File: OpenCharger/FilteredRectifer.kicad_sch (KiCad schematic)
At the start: 6 parts, among them Q1 IPT015N10N5, Q2 IPT015N10N5, Q3 IPT015N10N5, Q4 IPT015N10N5

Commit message: updated
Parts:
- added C12, C13, C5, C9: 100uF, Capacitor_THT:CP_Radial_D16.0mm_P7.50mm, symbol Device:C_Polarized_US
- added D2, D3: D_Zener, symbol Device:D_Zener
- added Q10, Q11, Q12, Q13, Q14, Q15, Q16, Q17: IPT015N10N5, Package_TO_SOT_SMD:Infineon_PG-HSOF-8-1, symbol Transistor_FET:IPT015N10N5
- added R14, R15, R2, R4: R_US, Resistor_SMD:R_0603_1608Metric, symbol Device:R_US
- added R3: R_Small_US, symbol Device:R_Small_US
- added U4: MCP6L01x-xLT, Package_TO_SOT_SMD:SOT-353_SC-70-5, symbol Amplifier_Operational:MCP6L01x-xLT
- C3, C4: value 56uF -> 100uF; footprint Capacitor_THT:CP_Radial_D40.0mm_P10.00mm_SnapIn -> Capacitor_THT:CP_Radial_D16.0mm_P7.50mm
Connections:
- net V_{in}+: now also Q10.3 (D), R2.1; no longer Q1.3 (D)
- net V_{in}-: now also Q15.2 (S), R4.2; no longer Q2.2 (S)
- net V_{out}+: now also Q1.3 (D), C12.1, C13.1, C5.1, C9.1, Q13.3 (D); no longer Q2.3 (D), Q3.3 (D)
- net V_{out}-: now also C12.2, C13.2, C5.2, C9.2, D2.2 (A), D3.2 (A), Q12.2 (S), Q17.2 (S), R14.2, R15.1, U4.2 (V-); no longer Q1.2 (S), Q4.2 (S)
- net PHG2: now reaches Q1.1 (G)
- net PHG0: now reaches Q3.1 (G)
- net NLG2: now reaches Q4.1 (G)
- net PHG1: now reaches Q2.1 (G)
- new net: D3.1 (K), R15.2, R3.2, R4.1, U4.4 (-)
- new net: D2.1 (K), R14.1, R2.2, R3.1, U4.3 (+)
- new net 3v3: U4.5 (V+)
- new net FORWARD: U4.1
- new net NHG0: Q15.1 (G)
- new net NHG1: Q14.1 (G)
- new net NHG2: Q13.1 (G)
- new net NHS1: Q14.2 (S), Q15.3 (D)
- new net NHS2: Q13.2 (S), Q14.3 (D)
- new net NLG0: Q17.1 (G)
- new net NLG1: Q16.1 (G)
- new net NLS1: Q16.2 (S), Q17.3 (D)
- new net NLS2: Q16.3 (D), Q4.2 (S)
- new net PHS1: Q2.2 (S), Q3.3 (D)
- new net PHS2: Q1.2 (S), Q2.3 (D)
- new net PLG0: Q12.1 (G)
- new net PLG1: Q11.1 (G)
- new net PLG2: Q10.1 (G)
- new net PLS1: Q11.2 (S), Q12.3 (D)
- new net PLS2: Q10.2 (S), Q11.3 (D)
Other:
- added sheet Rectifier Gate Drivers (RectifierGateDrivers.kicad_sch)
- note added: "Diode Enable"
- moved on the sheet: Q3, Q4

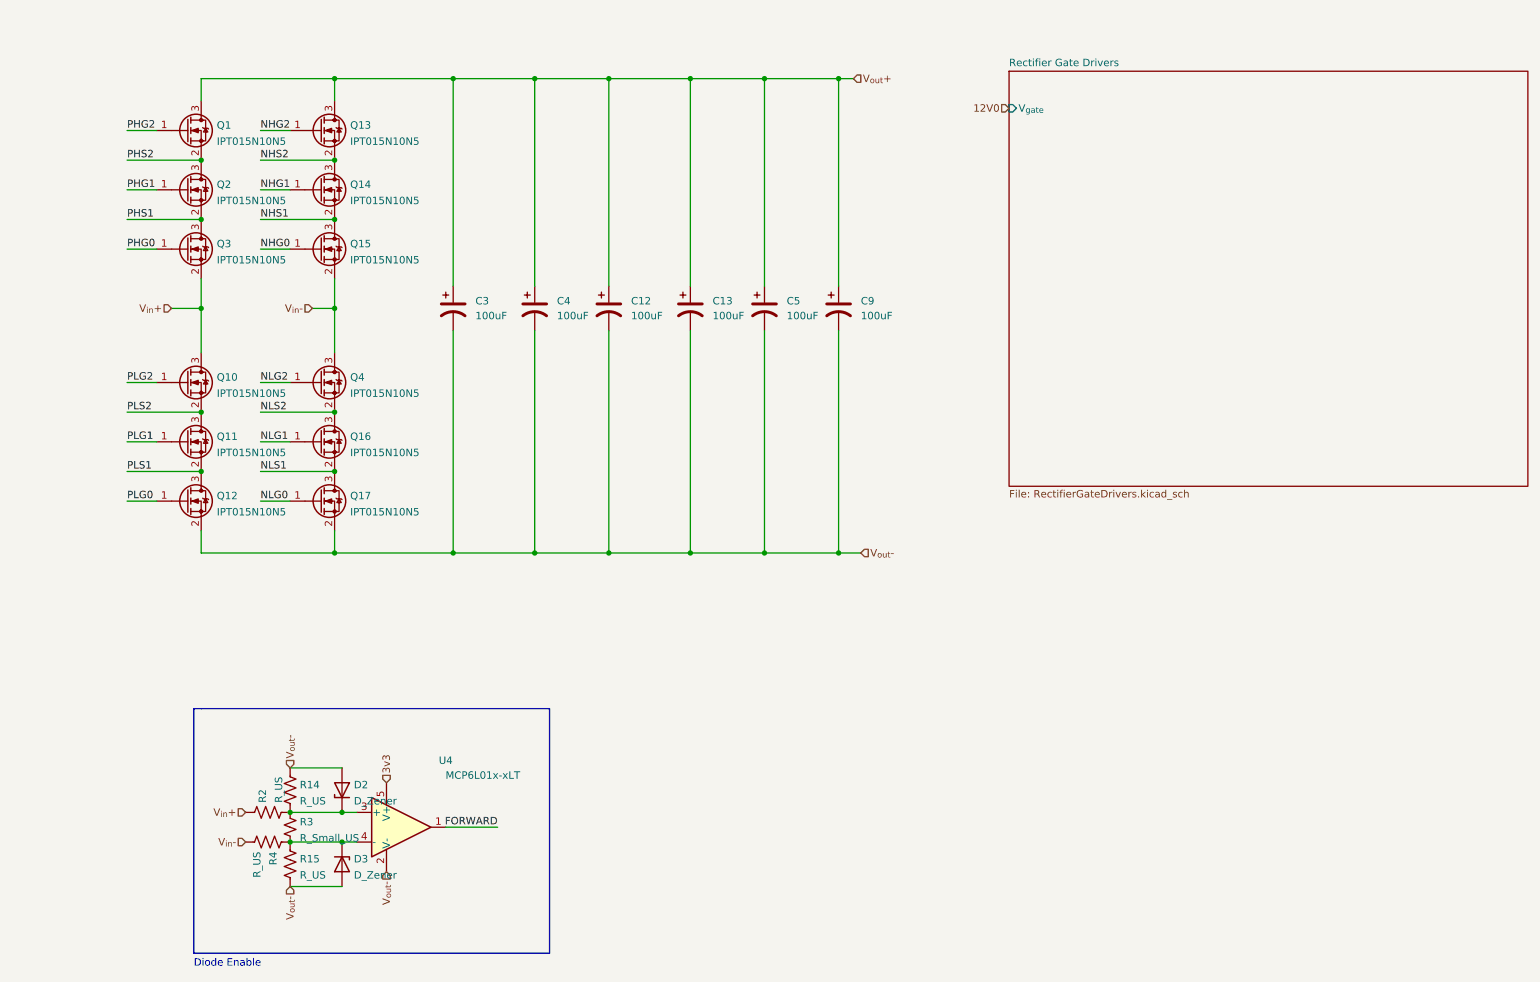
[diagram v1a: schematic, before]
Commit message: Updated Charger and MC
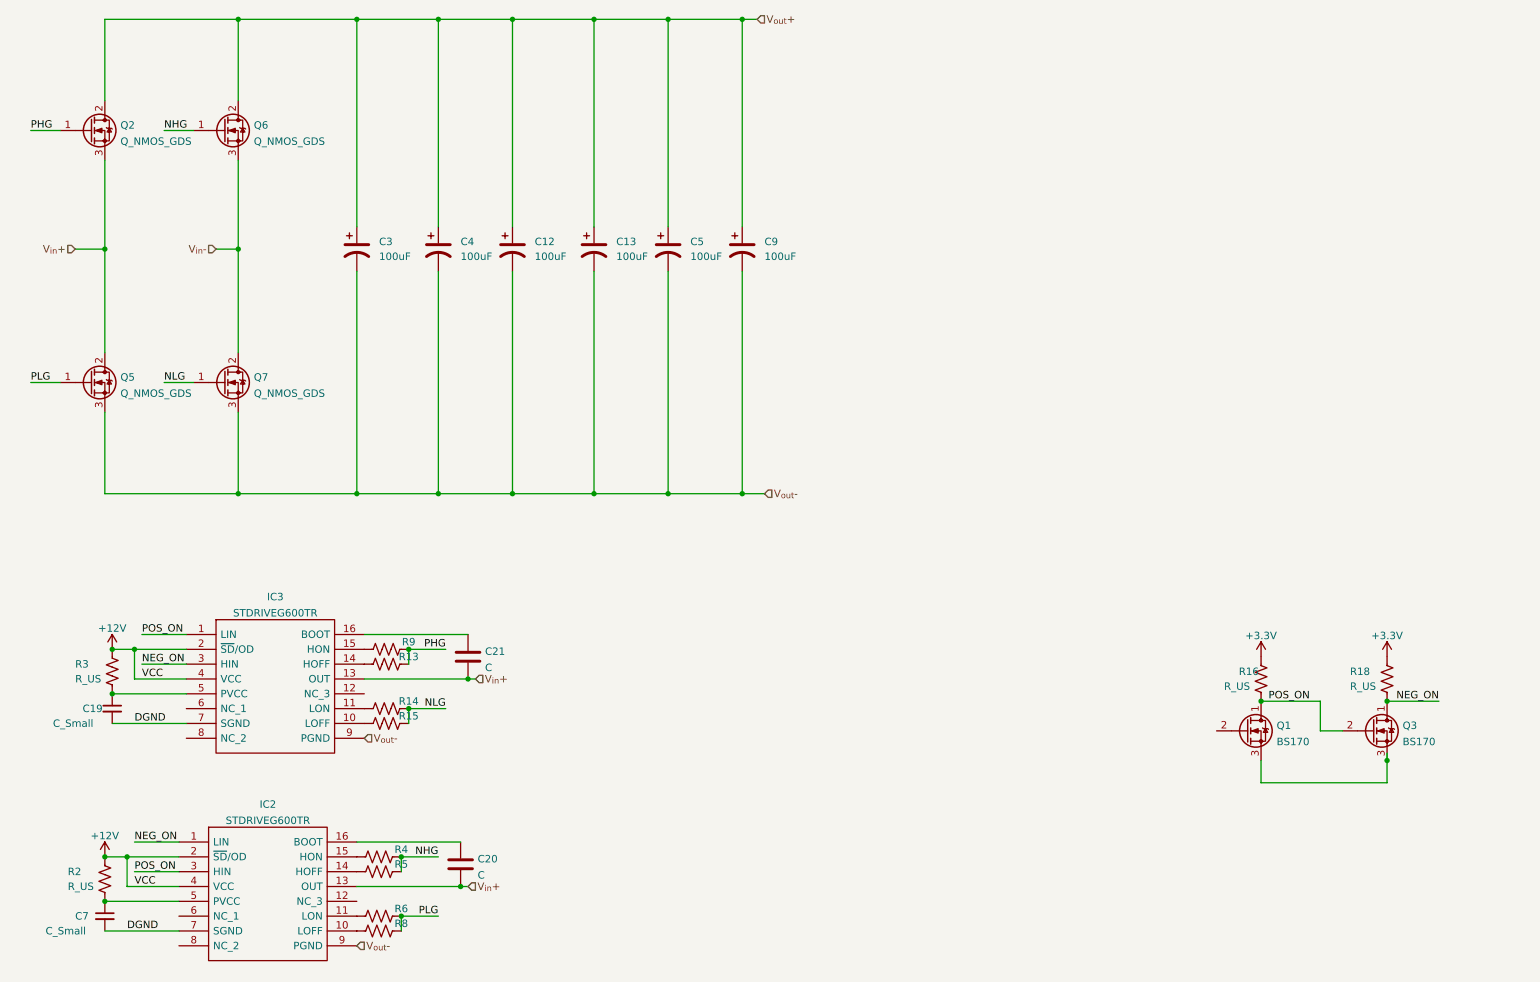
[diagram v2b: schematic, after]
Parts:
- removed D2, D3: D_Zener, symbol Device:D_Zener
- removed Q1, Q10, Q11, Q12, Q13, Q14, Q15, Q16, Q17, Q2, Q3, Q4: IPT015N10N5, Package_TO_SOT_SMD:Infineon_PG-HSOF-8-1, symbol Transistor_FET:IPT015N10N5
- removed R3: R_Small_US, symbol Device:R_Small_US
- removed U4: MCP6L01x-xLT, Package_TO_SOT_SMD:SOT-353_SC-70-5, symbol Amplifier_Operational:MCP6L01x-xLT
- added C19, C7: C_Small, symbol Device:C_Small
- added C20, C21: C, symbol Device:C
- added IC2, IC3: STDRIVEG600TR, SOIC127P600X175-16N, symbol SamacSys_Parts:STDRIVEG600TR
- added Q1, Q3: BS170, Package_TO_SOT_THT:TO-92_Inline, symbol Transistor_FET:BS170
- added Q2, Q5, Q6, Q7: Q_NMOS_GDS, Package_TO_SOT_SMD:TO-263-3_TabPin2, symbol Device:Q_NMOS_GDS
- added R13, R5, R6, R8, R9: 10, Resistor_SMD:R_1206_3216Metric, symbol Device:R_US
- added R16, R18: R_US, Resistor_SMD:R_0603_1608Metric, symbol Device:R_US
- added R3: R_US, symbol Device:R_US
- R14, R15, R4: value R_US -> 10; footprint Resistor_SMD:R_0603_1608Metric -> Resistor_SMD:R_1206_3216Metric
- R2: footprint Resistor_SMD:R_0603_1608Metric -> (none)
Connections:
- net V_{in}+: now also C20.2, C21.2, IC2.13 (OUT), IC3.13 (OUT), Q2.3 (S), Q5.2 (D); no longer R2.1
- net V_{in}-: now also Q6.3 (S), Q7.2 (D); no longer R4.2
- net V_{out}+: now also Q2.2 (D), Q6.2 (D)
- net V_{out}-: now also IC2.9 (PGND), IC3.9 (PGND), Q5.3 (S), Q7.3 (S); no longer R14.2, R15.1
- net at R15.2: now also IC3.10 (LOFF); no longer R4.1
- net at R2.2: now also C7.1, IC2.5 (PVCC); no longer R14.1
- new net: IC3.15 (HON), R9.2
- new net: IC2.11 (LON), R6.2
- new net: IC2.15 (HON), R4.2
- new net: Q1.3 (S), Q3.3 (S)
- new net: IC3.11 (LON), R14.2
- new net: IC3.14 (HOFF), R13.2
- new net: C21.1, IC3.16 (BOOT)
- new net: C19.1, IC3.5 (PVCC), R3.2
- new net: IC2.14 (HOFF), R5.2
- new net: IC2.10 (LOFF), R8.2
- new net: C20.1, IC2.16 (BOOT)
- new net +12V: IC2.2 (~{SD}/OD), IC2.4 (VCC), IC3.2 (~{SD}/OD), IC3.4 (VCC), R2.1, R3.1
- new net +3V3: R16.1, R18.1
- new net DGND: C19.2, C7.2, IC2.7 (SGND), IC3.7 (SGND)
- new net NEG_ON: IC2.1 (LIN), IC3.3 (HIN), Q3.1 (D), R18.2
- new net NHG: Q6.1 (G), R4.1, R5.1
- new net NLG: Q7.1 (G), R14.1, R15.1
- new net PHG: Q2.1 (G), R13.1, R9.1
- new net PLG: Q5.1 (G), R6.1, R8.1
- new net POS_ON: IC2.3 (HIN), IC3.1 (LIN), Q1.1 (D), Q3.2 (G), R16.2
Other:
- removed sheet Rectifier Gate Drivers
- note removed: "Diode Enable"
- moved on the sheet: C12, C13, C3, C4, C5, C9
